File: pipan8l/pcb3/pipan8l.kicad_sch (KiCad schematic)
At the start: 64 parts, among them J1 2x18edgecon, J2 2x18edgecon, J3 2x18edgecon, J4 2x18edgecon, J5 Conn_02x20_Odd_Even, J6 Conn_01x02_Pin, J7 Conn_01x16, J8 Conn_01x12, Q1 2N3906, Q10 2N3906, Q11 2N3906, Q12 2N3906, Q13 2N3906, Q14 2N3906, Q15 2N3906, Q16 2N3906, Q17 2N7000, Q18 2N7000, Q2 2N3906, Q3 2N3906, Q4 2N3906, Q5 2N3906, Q6 2N3906, Q7 2N3906, Q8 2N3906, Q9 2N3906, U1 MCP23017, U2 MCP23017, U3 MCP23017, U4 MCP23017

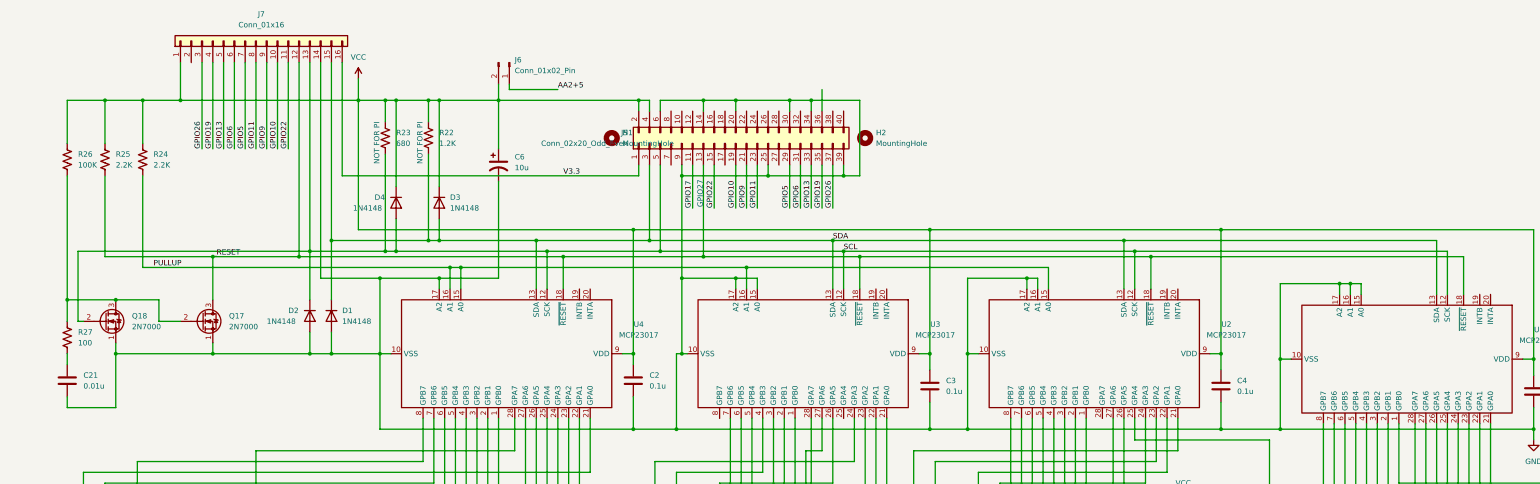
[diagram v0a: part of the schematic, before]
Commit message: revert pipan8l/pcb3 front-panel piggy-back board to 2025-01-02
it is good enough as is and don't want to make new boards
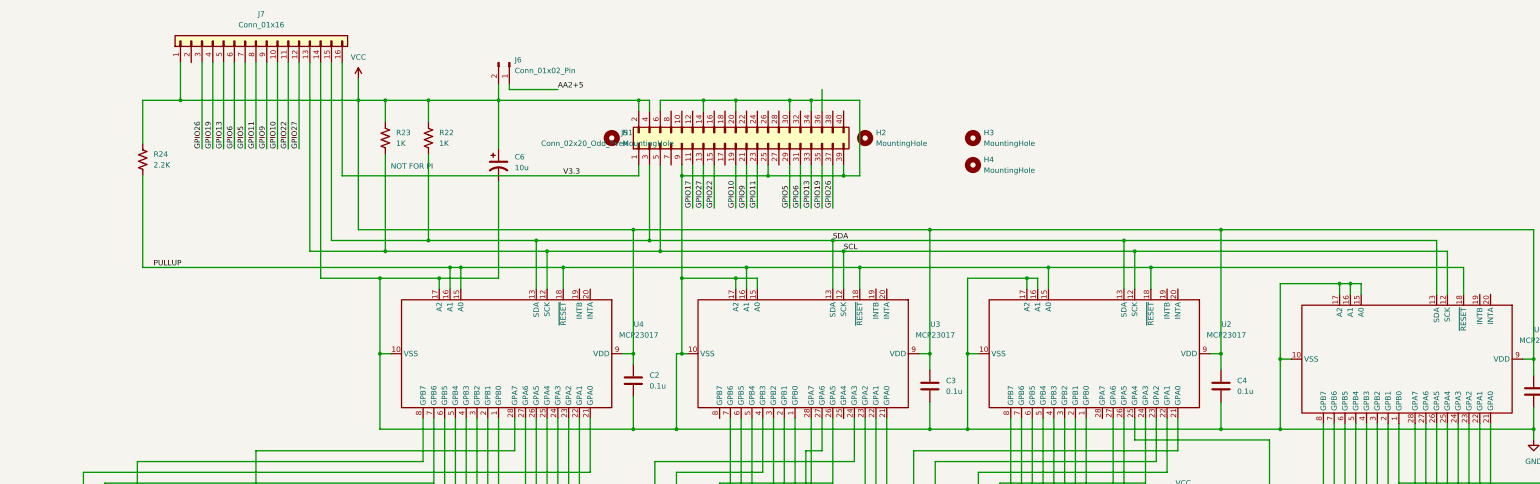
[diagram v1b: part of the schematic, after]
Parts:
- removed C21: 0.01u, Capacitor_THT:C_Axial_L3.8mm_D2.6mm_P7.50mm_Horizontal, symbol Device:C
- removed D1, D2, D3, D4: 1N4148, Diode_THT:D_DO-35_SOD27_P7.62mm_Horizontal, symbol Diode:1N4148
- removed Q17, Q18: 2N7000, Package_TO_SOT_THT:TO-92_Inline_W4.0mm_Horizontal_FlatSideDown, symbol Transistor_FET:2N7000
- removed R25: 2.2K, Resistor_THT:R_Axial_DIN0207_L6.3mm_D2.5mm_P10.16mm_Horizontal, symbol Device:R_US
- removed R26: 100K, Resistor_THT:R_Axial_DIN0207_L6.3mm_D2.5mm_P10.16mm_Horizontal, symbol Device:R_US
- removed R27: 100, Resistor_THT:R_Axial_DIN0207_L6.3mm_D2.5mm_P10.16mm_Horizontal, symbol Device:R_US
- added H3, H4: MountingHole, MountingHole:MountingHole_8.4mm_M8, symbol Mechanical:MountingHole
- J1: footprint myz8lfpanfoots:backpins-A -> mypipan8lfoots:backpins-A; symbol myz8lfpanlib:2x18edgecon -> mypipan8llib:2x18edgecon
- J2: footprint myz8lfpanfoots:backpins-B -> mypipan8lfoots:backpins-B; symbol myz8lfpanlib:2x18edgecon -> mypipan8llib:2x18edgecon
- J3: footprint myz8lfpanfoots:backpins-C -> mypipan8lfoots:backpins-C; symbol myz8lfpanlib:2x18edgecon -> mypipan8llib:2x18edgecon
- J4: footprint myz8lfpanfoots:backpins-D -> mypipan8lfoots:backpins-D; symbol myz8lfpanlib:2x18edgecon -> mypipan8llib:2x18edgecon
- R22: value 1.2K -> 1K
- R23: value 680 -> 1K
- U1, U2, U3, U4: symbol myz8lfpanlib:MCP23017 -> mypipan8llib:MCP23017
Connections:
- net PULLUP: now also U1.18 (~{RESET}), U2.18 (~{RESET}), U3.18 (~{RESET}), U4.18 (~{RESET})
- removed net _RESET: J5.13 (Pin_13), J7.12 (Pin_12), U1.18 (~{RESET}), U2.18 (~{RESET}), U3.18 (~{RESET}), U4.18 (~{RESET})
- new net GPIO27: J5.13 (Pin_13), J7.12 (Pin_12)
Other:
- note removed: "GPIO27"

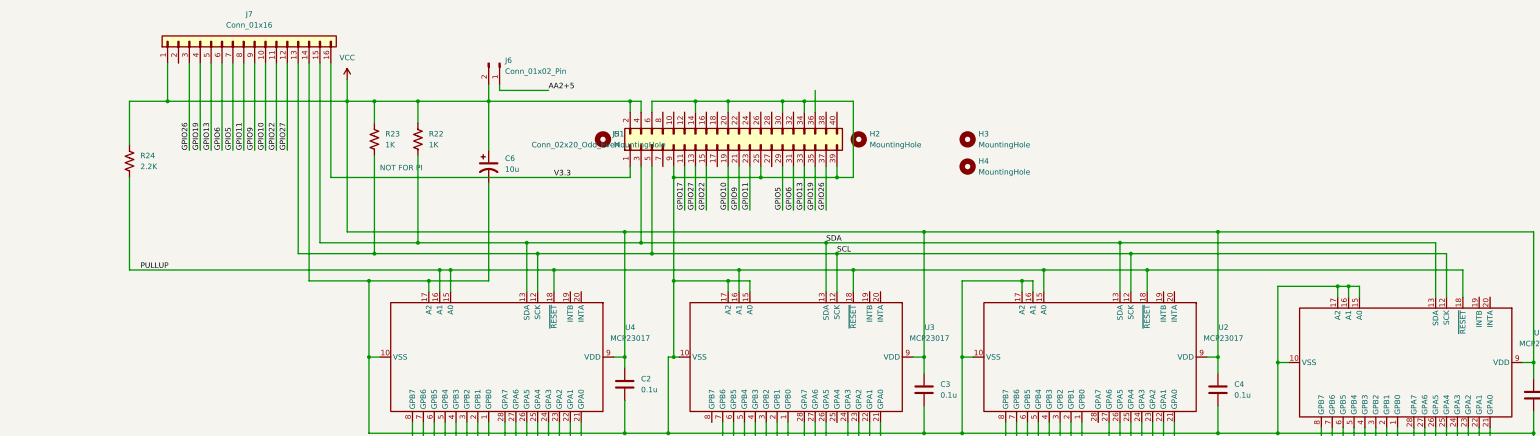
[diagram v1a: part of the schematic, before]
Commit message: add clipping diodes to i2c bus for zynq-connected front panel
also add _RESET line as 4th pin on connector
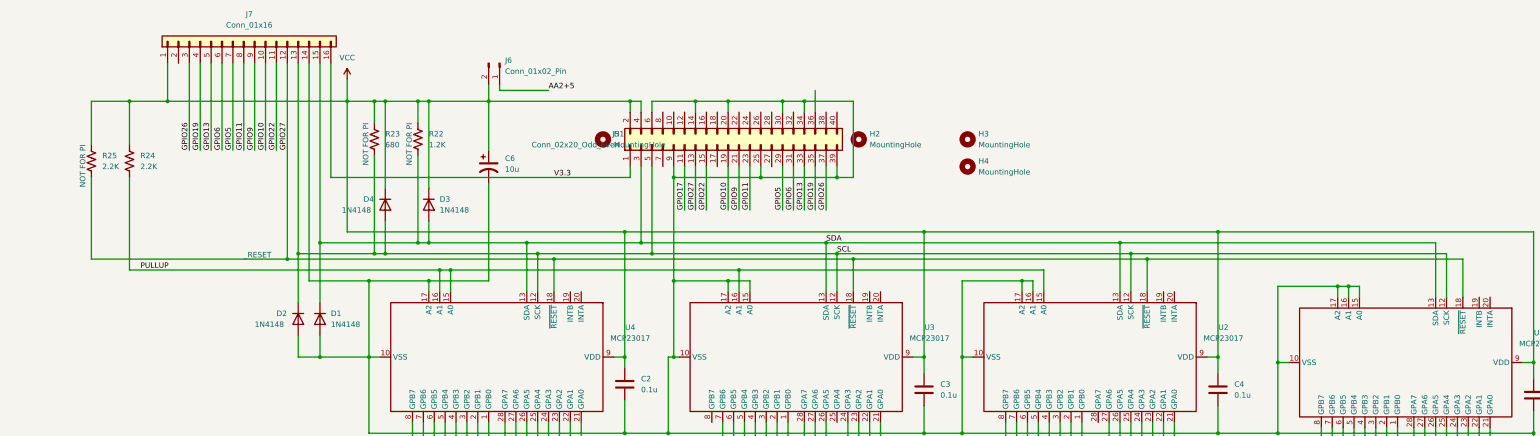
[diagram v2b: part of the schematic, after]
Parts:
- added D1, D2, D3, D4: 1N4148, Diode_THT:D_DO-35_SOD27_P7.62mm_Horizontal, symbol Diode:1N4148
- added R25: 2.2K, Resistor_THT:R_Axial_DIN0207_L6.3mm_D2.5mm_P10.16mm_Horizontal, symbol Device:R_US
- R22: value 1K -> 1.2K
- R23: value 1K -> 680
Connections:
- net GND: now also D1.2 (A), D2.2 (A)
- net GPIO27: now also U1.18 (~{RESET}), U2.18 (~{RESET}), U3.18 (~{RESET}), U4.18 (~{RESET}), R25.2
- net PULLUP: no longer U1.18 (~{RESET}), U2.18 (~{RESET}), U3.18 (~{RESET}), U4.18 (~{RESET})
- net SCL: now also D2.1 (K), D4.2 (A)
- net SDA: now also D1.1 (K), D3.2 (A)
- net VCC: now also D3.1 (K), D4.1 (K), R25.1
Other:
- note added: "_RESET"

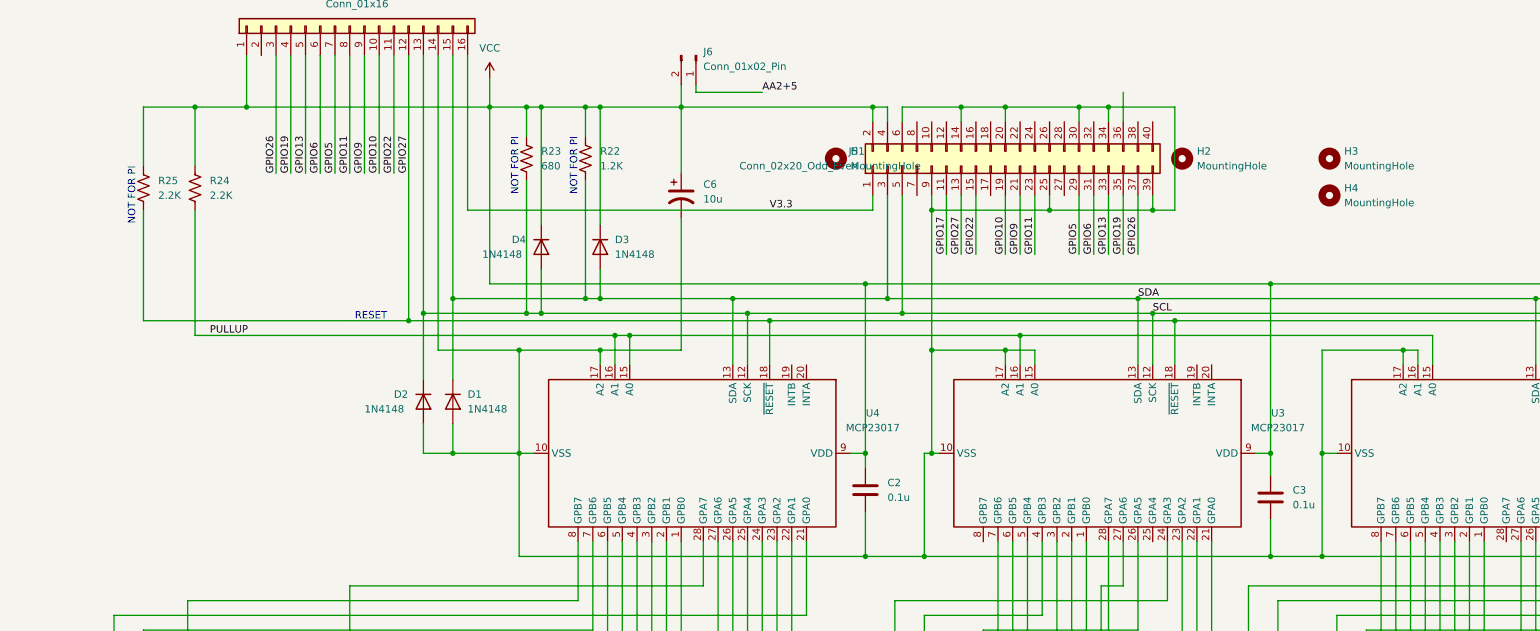
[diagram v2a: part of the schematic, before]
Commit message: update pipan8l pcb3 reset circuit
hold clock low for 1mS to trigger reset
do not need 4th wire though pins are still there
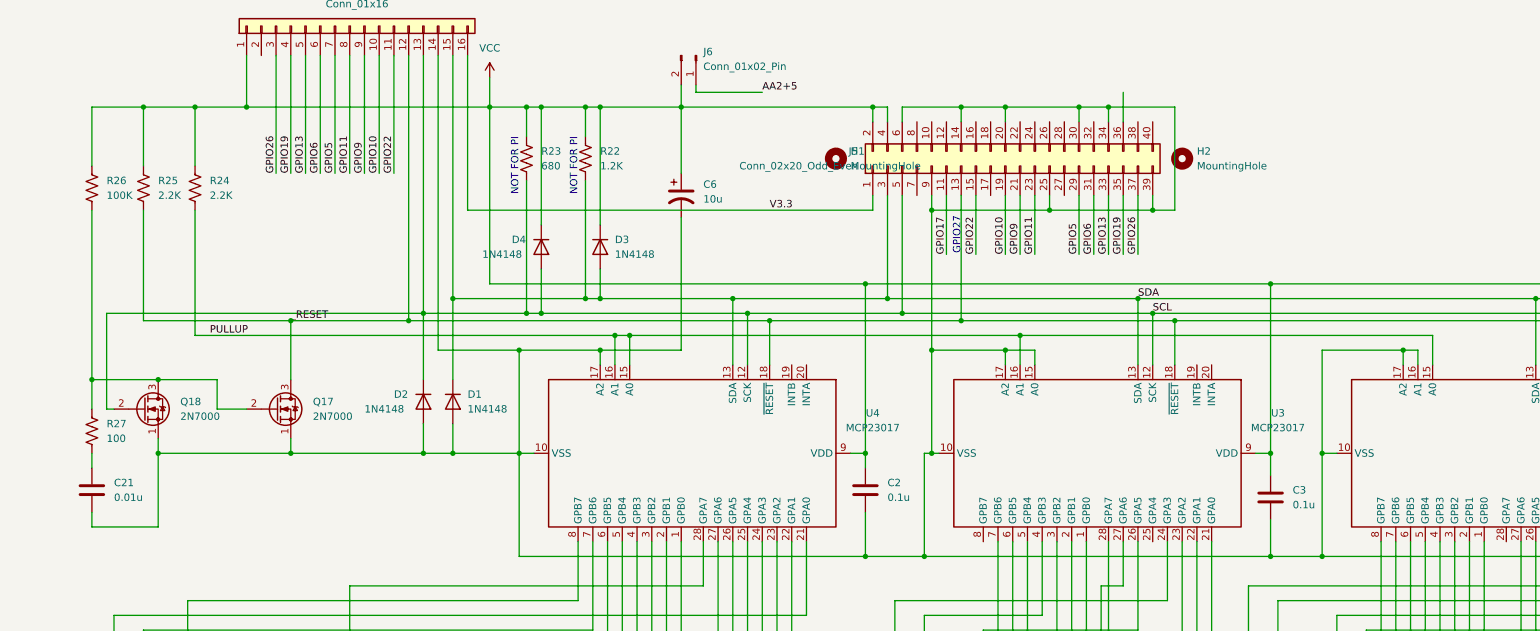
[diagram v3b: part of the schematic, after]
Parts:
- removed H3, H4: MountingHole, MountingHole:MountingHole_8.4mm_M8, symbol Mechanical:MountingHole
- added C21: 0.01u, Capacitor_THT:C_Axial_L3.8mm_D2.6mm_P7.50mm_Horizontal, symbol Device:C
- added Q17, Q18: 2N7000, Package_TO_SOT_THT:TO-92_Inline_W4.0mm_Horizontal_FlatSideDown, symbol Transistor_FET:2N7000
- added R26: 100K, Resistor_THT:R_Axial_DIN0207_L6.3mm_D2.5mm_P10.16mm_Horizontal, symbol Device:R_US
- added R27: 100, Resistor_THT:R_Axial_DIN0207_L6.3mm_D2.5mm_P10.16mm_Horizontal, symbol Device:R_US
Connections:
- net GND: now also C21.2, Q17.1 (S), Q18.1 (S)
- net SCL: now also Q18.2 (G)
- net VCC: now also R26.1
- net GPIO27 renamed _RESET
- net _RESET: now also Q17.3 (D)
- new net: Q17.2 (G), Q18.3 (D), R26.2, R27.1
- new net: C21.1, R27.2
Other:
- note added: "GPIO27"
- note removed: "_RESET"
